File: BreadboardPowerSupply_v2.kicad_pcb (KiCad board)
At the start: 2 copper layers, 30.1 x 52.2 mm, 15 parts, among them J1 Barrel_Jack_Switch, J2 Conn_02x02_Odd_Even, J3 Conn_02x02_Odd_Even, SW1 SW_DPDT_x2, U1 LM7805_TO220

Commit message: Placement completed.
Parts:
- C1: footprint Capacitor_THT:CP_Radial_D10.0mm_P5.00mm_P7.50mm -> Capacitor_THT:CP_Radial_D10.0mm_P5.00mm
- moved C1 48.8 mm to (43.3, 110.6), turned to 270 degrees
- moved D1 10.9 mm to (39.1, 144.7)
- moved D4 10.5 mm to (39.1, 130.4)
- moved R2 7.62 mm to (50.8, 119.6), turned to 270 degrees
- moved D2 4.62 mm to (39.1, 139.9)
- moved U1 4.57 mm to (40.6, 123.7)
- moved C2 2.22 mm to (54.2, 112.0), turned to 270 degrees
- moved D3 2.16 mm to (39.1, 135.2)
- moved D6 0.13 mm to (55.0, 121.8)

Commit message: Added additional net names for power.
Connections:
- net /Vout renamed /Vout1
- net Net-(D1-Pad2) renamed /V1
- net Net-(D3-Pad2) renamed /V2
- net Net-(J2-Pad1) renamed /Vout2
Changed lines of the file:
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@@
   (net 1 /Vin)
   (net 2 /V-)
-  (net 3 /Vout)
-  (net 4 "Net-(D1-Pad2)")
-  (net 5 "Net-(D3-Pad2)")
-  (net 6 "Net-(D5-Pad2)")
-  (net 7 "Net-(D6-Pad2)")
-  (net 8 "Net-(J1-Pad3)")
-  (net 9 "Net-(J2-Pad1)")
-  (net 10 "Net-(SW1-Pad3)")
+  (net 3 "Net-(D5-Pad2)")
+  (net 4 "Net-(D6-Pad2)")
+  (net 5 "Net-(J1-Pad3)")
+  (net 6 "Net-(SW1-Pad3)")
+  (net 7 /V1)
+  (net 8 /V2)
+  (net 9 /Vout2)
+  (net 10 /Vout1)
   (net_class Default "This is the default net class."
     (clearance 0.2)
@@
     (uvia_drill 0.1)
     (add_net /V-)
+    (add_net /V1)
+    (add_net /V2)
     (add_net /Vin)
-    (add_net /Vout)
-    (add_net "Net-(D1-Pad2)")
-    (add_net "Net-(D3-Pad2)")
+    (add_net /Vout1)
+    (add_net /Vout2)
     (add_net "Net-(D5-Pad2)")
     (add_net "Net-(D6-Pad2)")
     (add_net "Net-(J1-Pad3)")
-    (add_net "Net-(J2-Pad1)")
     (add_net "Net-(SW1-Pad3)")
   )
@@
     )
     (pad 1 thru_hole rect (at 0 0 270) (size 1.6 1.6) (drill 0.8) (layers *.Cu *.Mask)
-      (net 3 /Vout))
+      (net 10 /Vout1))
     (pad 2 thru_hole circle (at 2.5 0 270) (size 1.6 1.6) (drill 0.8) (layers *.Cu *.Mask)
       (net 2 /V-))
@@
       (net 1 /Vin))
     (pad 2 thru_hole oval (at 10.16 0) (size 2.2 2.2) (drill 1.1) (layers *.Cu *.Mask)
-      (net 4 "Net-(D1-Pad2)"))
+      (net 7 /V1))
     (model ${KISYS3DMOD}/Diode_THT.3dshapes/D_DO-41_SOD81_P10.16mm_Horizontal.wrl
       (at (xyz 0 0 0))
@@
       (net 2 /V-))
     (pad 1 thru_hole rect (at 0 0) (size 2.2 2.2) (drill 1.1) (layers *.Cu *.Mask)
-      (net 4 "Net-(D1-Pad2)"))
+      (net 7 /V1))
     (model ${KISYS3DMOD}/Diode_THT.3dshapes/D_DO-41_SOD81_P10.16mm_Horizontal.wrl
       (at (xyz 0 0 0))
@@
       (net 1 /Vin))
     (pad 2 thru_hole oval (at 10.16 0) (size 2.2 2.2) (drill 1.1) (layers *.Cu *.Mask)
-      (net 5 "Net-(D3-Pad2)"))
+      (net 8 /V2))
     (model ${KISYS3DMOD}/Diode_THT.3dshapes/D_DO-41_SOD81_P10.16mm_Horizontal.wrl
       (at (xyz 0 0 0))
@@
       (net 2 /V-))
     (pad 1 thru_hole rect (at 0 0) (size 2.2 2.2) (drill 1.1) (layers *.Cu *.Mask)
-      (net 5 "Net-(D3-Pad2)"))
+      (net 8 /V2))
     (model ${KISYS3DMOD}/Diode_THT.3dshapes/D_DO-41_SOD81_P10.16mm_Horizontal.wrl
       (at (xyz 0 0 0))
@@
     (fp_arc (start 1.27 0) (end -1.23 -1.469694) (angle 299.1) (layer F.Fab) (width 0.1))
     (pad 2 thru_hole circle (at 2.54 0) (size 1.8 1.8) (drill 0.9) (layers *.Cu *.Mask)
-      (net 6 "Net-(D5-Pad2)"))
+      (net 3 "Net-(D5-Pad2)"))
     (pad 1 thru_hole rect (at 0 0) (size 1.8 1.8) (drill 0.9) (layers *.Cu *.Mask)
       (net 2 /V-))
@@
       (net 2 /V-))
     (pad 2 thru_hole circle (at 2.54 0) (size 1.8 1.8) (drill 0.9) (layers *.Cu *.Mask)
-      (net 7 "Net-(D6-Pad2)"))
+      (net 4 "Net-(D6-Pad2)"))
     (model ${KISYS3DMOD}/LED_THT.3dshapes/LED_D5.0mm.wrl
       (at (xyz 0 0 0))
@@
     (fp_line (start -4.5 10.2) (end 4.5 10.2) (layer F.Fab) (width 0.1))
     (pad 1 thru_hole rect (at 0 0 270) (size 2.6 2.6) (drill 1.6) (layers *.Cu *.Mask)
-      (net 4 "Net-(D1-Pad2)"))
+      (net 7 /V1))
     (pad 2 thru_hole circle (at 0 6 270) (size 2.6 2.6) (drill 1.6) (layers *.Cu *.Mask)
-      (net 5 "Net-(D3-Pad2)"))
+      (net 8 /V2))
     (pad 3 thru_hole circle (at 4.7 3 270) (size 2.6 2.6) (drill 1.6) (layers *.Cu *.Mask)
-      (net 8 "Net-(J1-Pad3)"))
+      (net 5 "Net-(J1-Pad3)"))
     (model ${KISYS3DMOD}/Connector_BarrelJack.3dshapes/BarrelJack_CUI_PJ-102AH_Horizontal.wrl
       (at (xyz 0 0 0))
@@
       (net 2 /V-))
     (pad 2 thru_hole oval (at 2.54 0 180) (size 1.7 1.7) (drill 1) (layers *.Cu *.Mask)
-      (net 9 "Net-(J2-Pad1)"))
+      (net 9 /Vout2))
     (pad 1 thru_hole rect (at 0 0 180) (size 1.7 1.7) (drill 1) (layers *.Cu *.Mask)
-      (net 9 "Net-(J2-Pad1)"))
+      (net 9 /Vout2))
     (model ${KISYS3DMOD}/Connector_PinHeader_2.54mm.3dshapes/PinHeader_2x02_P2.54mm_Vertical.wrl
       (at (xyz 0 0 0))
@@
     )
     (pad 1 thru_hole rect (at 0 0 180) (size 1.7 1.7) (drill 1) (layers *.Cu *.Mask)
-      (net 9 "Net-(J2-Pad1)"))
+      (net 9 /Vout2))
     (pad 2 thru_hole oval (at 2.54 0 180) (size 1.7 1.7) (drill 1) (layers *.Cu *.Mask)
-      (net 9 "Net-(J2-Pad1)"))
+      (net 9 /Vout2))
     (pad 3 thru_hole oval (at 0 2.54 180) (size 1.7 1.7) (drill 1) (layers *.Cu *.Mask)
       (net 2 /V-))
@@
     )
     (pad 1 thru_hole circle (at 0 0 90) (size 1.6 1.6) (drill 0.8) (layers *.Cu *.Mask)
-      (net 3 /Vout))
+      (net 10 /Vout1))
     (pad 2 thru_hole oval (at 7.62 0 90) (size 1.6 1.6) (drill 0.8) (layers *.Cu *.Mask)
-      (net 6 "Net-(D5-Pad2)"))
+      (net 3 "Net-(D5-Pad2)"))
     (model ${KISYS3DMOD}/Resistor_THT.3dshapes/R_Axial_DIN0207_L6.3mm_D2.5mm_P7.62mm_Horizontal.wrl
       (at (xyz 0 0 0))
@@
     (fp_line (start 0.66 -1.25) (end 0.66 1.25) (layer F.Fab) (width 0.1))
     (pad 2 thru_hole oval (at 7.62 0 270) (size 1.6 1.6) (drill 0.8) (layers *.Cu *.Mask)
-      (net 7 "Net-(D6-Pad2)"))
+      (net 4 "Net-(D6-Pad2)"))
     (pad 1 thru_hole circle (at 0 0 270) (size 1.6 1.6) (drill 0.8) (layers *.Cu *.Mask)
-      (net 9 "Net-(J2-Pad1)"))
+      (net 9 /Vout2))
     (model ${KISYS3DMOD}/Resistor_THT.3dshapes/R_Axial_DIN0207_L6.3mm_D2.5mm_P7.62mm_Horizontal.wrl
       (at (xyz 0 0 0))
@@
     (fp_line (start -3.42 -2) (end 8.18 -2) (layer F.Fab) (width 0.1))
     (pad 1 thru_hole rect (at 0 0 90) (size 1.9 1.9) (drill 0.9) (layers *.Cu *.Mask)
-      (net 9 "Net-(J2-Pad1)"))
+      (net 9 /Vout2))
     (pad 2 thru_hole circle (at 2.5 0 90) (size 1.9 1.9) (drill 0.9) (layers *.Cu *.Mask)
-      (net 3 /Vout))
+      (net 10 /Vout1))
     (pad 3 thru_hole circle (at 5 0 90) (size 1.9 1.9) (drill 0.9) (layers *.Cu *.Mask)
-      (net 10 "Net-(SW1-Pad3)"))
+      (net 6 "Net-(SW1-Pad3)"))
   )
   (module Package_TO_SOT_THT:TO-220-3_Vertical (layer F.Cu)
@@
       (net 2 /V-))
     (pad 3 thru_hole oval (at 5.08 0) (size 1.905 2) (drill 1.1) (layers *.Cu *.Mask)
-      (net 3 /Vout))
+      (net 10 /Vout1))
     (model ${KISYS3DMOD}/Package_TO_SOT_THT.3dshapes/TO-220-3_Vertical.wrl
       (at (xyz 0 0 0))

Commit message: Tracing is complete.
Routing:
- net /V-: track 0.00 -> 89.2 mm
- net /Vout2: track 0.00 -> 69.1 mm
- net /Vout1: track 0.00 -> 59.3 mm
- net /Vin: track 0.00 -> 39.6 mm
- net /V2: track 0.00 -> 30.3 mm
- net /V1: track 0.00 -> 21.0 mm
- net Net-(D6-Pad2): track 0.00 -> 9.74 mm
- net Net-(D5-Pad2): track 0.00 -> 7.17 mm
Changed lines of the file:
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@@
     (thickness 1.6)
     (drawings 13)
-    (tracks 0)
+    (tracks 93)
     (zones 0)
     (modules 15)
@@
     (uvia_dia 0.3)
     (uvia_drill 0.1)
-    (add_net /V-)
-    (add_net /V1)
-    (add_net /V2)
-    (add_net /Vin)
-    (add_net /Vout1)
-    (add_net /Vout2)
     (add_net "Net-(D5-Pad2)")
     (add_net "Net-(D6-Pad2)")
@@
     (uvia_dia 0.3)
     (uvia_drill 0.1)
+    (add_net /V-)
+    (add_net /V1)
+    (add_net /V2)
+    (add_net /Vin)
+    (add_net /Vout1)
+    (add_net /Vout2)
   )
   (module Capacitor_THT:CP_Radial_D6.3mm_P2.50mm (layer F.Cu)
@@
   (gr_line (start 36.957 159.385) (end 67.056 159.385) (layer Edge.Cuts) (width 0.15))
   (gr_line (start 36.957 107.188) (end 36.957 159.385) (layer Edge.Cuts) (width 0.15))
+  (segment (start 37.48201 141.61901) (end 39.116 143.253) (width 0.3) (layer F.Cu) (net 1))
+  (segment (start 37.48201 138.204323) (end 37.48201 141.61901) (width 0.3) (layer F.Cu) (net 1))
+  (segment (start 39.116 136.570333) (end 37.48201 138.204323) (width 0.3) (layer F.Cu) (net 1))
+  (segment (start 39.116 143.253) (end 39.116 144.653) (width 0.3) (layer F.Cu) (net 1))
+  (segment (start 39.116 135.170333) (end 39.116 136.570333) (width 0.3) (layer F.Cu) (net 1))
+  (segment (start 39.116 133.770333) (end 42.164 130.722333) (width 0.3) (layer F.Cu) (net 1))
+  (segment (start 39.116 135.170333) (end 39.116 133.770333) (width 0.3) (layer F.Cu) (net 1))
+  (segment (start 42.164 130.722333) (end 42.164 127.889) (width 0.3) (layer F.Cu) (net 1))
+  (segment (start 40.64 126.365) (end 40.64 123.698) (width 0.3) (layer F.Cu) (net 1))
+  (segment (start 42.164 127.889) (end 40.64 126.365) (width 0.3) (layer F.Cu) (net 1))
+  (segment (start 42.007 110.617) (end 43.307 110.617) (width 0.3) (layer F.Cu) (net 1))
+  (segment (start 40.132 112.649) (end 41.783 110.998) (width 0.3) (layer F.Cu) (net 1))
+  (segment (start 40.64 122.398) (end 40.132 121.89) (width 0.3) (layer F.Cu) (net 1))
+  (segment (start 40.64 123.698) (end 40.64 122.398) (width 0.3) (layer F.Cu) (net 1))
+  (segment (start 40.132 121.89) (end 40.132 112.649) (width 0.3) (layer F.Cu) (net 1))
+  (segment (start 41.783 110.841) (end 42.007 110.617) (width 0.3) (layer F.Cu) (net 1))
+  (segment (start 41.783 110.998) (end 41.783 110.841) (width 0.3) (layer F.Cu) (net 1))
+  (segment (start 43.18 124.333) (end 43.18 123.698) (width 0.3) (layer B.Cu) (net 2))
+  (segment (start 49.276 130.429) (end 43.18 124.333) (width 0.3) (layer B.Cu) (net 2))
+  (segment (start 54.991 140.786) (end 54.991 141.986) (width 0.3) (layer B.Cu) (net 2))
+  (segment (start 54.116666 139.911666) (end 54.991 140.786) (width 0.3) (layer B.Cu) (net 2))
+  (segment (start 49.276 139.911666) (end 54.116666 139.911666) (width 0.3) (layer B.Cu) (net 2))
+  (segment (start 54.991 143.186) (end 59.055 147.25) (width 0.3) (layer B.Cu) (net 2))
+  (segment (start 54.991 141.986) (end 54.991 143.186) (width 0.3) (layer B.Cu) (net 2))
+  (segment (start 59.055 152.126476) (end 59.69 152.761476) (width 0.3) (layer B.Cu) (net 2))
+  (segment (start 59.055 147.25) (end 59.055 152.126476) (width 0.3) (layer B.Cu) (net 2))
+  (segment (start 59.69 152.761476) (end 59.69 153.797) (width 0.3) (layer B.Cu) (net 2))
+  (segment (start 60.579 154.686) (end 62.484 154.686) (width 0.3) (layer B.Cu) (net 2))
+  (segment (start 59.69 153.797) (end 60.579 154.686) (width 0.3) (layer B.Cu) (net 2))
+  (segment (start 62.484 154.686) (end 65.024 154.686) (width 0.3) (layer B.Cu) (net 2))
+  (segment (start 50.826001 138.361665) (end 50.826001 137.260999) (width 0.3) (layer B.Cu) (net 2))
+  (segment (start 49.276 139.911666) (end 50.826001 138.361665) (width 0.3) (layer B.Cu) (net 2))
+  (segment (start 50.826001 137.260999) (end 52.451 135.636) (width 0.3) (layer B.Cu) (net 2))
+  (segment (start 52.451 133.604) (end 49.276 130.429) (width 0.3) (layer B.Cu) (net 2))
+  (segment (start 52.451 135.636) (end 52.451 133.604) (width 0.3) (layer B.Cu) (net 2))
+  (segment (start 49.276 128.873366) (end 49.022 128.619366) (width 0.3) (layer B.Cu) (net 2))
+  (segment (start 49.276 130.429) (end 49.276 128.873366) (width 0.3) (layer B.Cu) (net 2))
+  (segment (start 49.022 128.619366) (end 49.022 125.349) (width 0.3) (layer B.Cu) (net 2))
+  (segment (start 52.578 121.793) (end 54.991 121.793) (width 0.3) (layer B.Cu) (net 2))
+  (segment (start 49.022 125.349) (end 52.578 121.793) (width 0.3) (layer B.Cu) (net 2))
+  (segment (start 54.991 115.276) (end 54.229 114.514) (width 0.3) (layer B.Cu) (net 2))
+  (segment (start 54.991 121.793) (end 54.991 115.276) (width 0.3) (layer B.Cu) (net 2))
+  (segment (start 43.18 115.744) (end 43.307 115.617) (width 0.3) (layer B.Cu) (net 2))
+  (segment (start 43.18 123.698) (end 43.18 115.744) (width 0.3) (layer B.Cu) (net 2))
+  (segment (start 54.229 114.514) (end 55.92 114.514) (width 0.3) (layer B.Cu) (net 2))
+  (segment (start 55.92 114.514) (end 60.706 109.728) (width 0.3) (layer B.Cu) (net 2))
+  (segment (start 60.706 109.728) (end 62.484 109.728) (width 0.3) (layer B.Cu) (net 2))
+  (segment (start 62.484 109.728) (end 65.024 109.728) (width 0.3) (layer B.Cu) (net 2))
+  (segment (start 56.769 148.844) (end 56.769 145.542) (width 0.25) (layer F.Cu) (net 3))
+  (segment (start 57.531 144.78) (end 57.531 141.986) (width 0.25) (layer F.Cu) (net 3))
+  (segment (start 56.769 145.542) (end 57.531 144.78) (width 0.25) (layer F.Cu) (net 3))
+  (segment (start 57.531 123.065792) (end 56.769 123.827792) (width 0.25) (layer F.Cu) (net 4))
+  (segment (start 57.531 121.793) (end 57.531 123.065792) (width 0.25) (layer F.Cu) (net 4))
+  (segment (start 54.226208 123.827792) (end 50.8 127.254) (width 0.25) (layer F.Cu) (net 4))
+  (segment (start 56.769 123.827792) (end 54.226208 123.827792) (width 0.25) (layer F.Cu) (net 4))
+  (segment (start 51.435 146.812) (end 49.276 144.653) (width 0.3) (layer F.Cu) (net 7))
+  (segment (start 51.435 152.654) (end 51.435 146.812) (width 0.3) (layer F.Cu) (net 7))
+  (segment (start 44.534666 139.911666) (end 39.116 139.911666) (width 0.3) (layer F.Cu) (net 7))
+  (segment (start 49.276 144.653) (end 44.534666 139.911666) (width 0.3) (layer F.Cu) (net 7))
+  (segment (start 45.435 139.011333) (end 49.276 135.170333) (width 0.3) (layer B.Cu) (net 8))
+  (segment (start 45.435 152.654) (end 45.435 139.011333) (width 0.3) (layer B.Cu) (net 8))
+  (segment (start 45.435 138.148) (end 45.435 139.011333) (width 0.3) (layer B.Cu) (net 8))
+  (segment (start 39.116 131.829) (end 45.435 138.148) (width 0.3) (layer B.Cu) (net 8))
+  (segment (start 39.116 130.429) (end 39.116 131.829) (width 0.3) (layer B.Cu) (net 8))
+  (segment (start 51.599999 118.834001) (end 54.774999 118.834001) (width 0.3) (layer F.Cu) (net 9))
+  (segment (start 50.8 119.634) (end 51.599999 118.834001) (width 0.3) (layer F.Cu) (net 9))
+  (segment (start 54.774999 118.834001) (end 59.309 114.3) (width 0.3) (layer F.Cu) (net 9))
+  (segment (start 59.309 114.3) (end 59.309 113.284) (width 0.3) (layer F.Cu) (net 9))
+  (segment (start 60.325 112.268) (end 62.484 112.268) (width 0.3) (layer F.Cu) (net 9))
+  (segment (start 59.309 113.284) (end 60.325 112.268) (width 0.3) (layer F.Cu) (net 9))
+  (segment (start 62.484 112.268) (end 65.024 112.268) (width 0.3) (layer F.Cu) (net 9))
+  (segment (start 59.309 132.441) (end 59.309 114.3) (width 0.3) (layer F.Cu) (net 9))
+  (segment (start 57.511 134.239) (end 59.309 132.441) (width 0.3) (layer F.Cu) (net 9))
+  (segment (start 56.261 134.239) (end 57.511 134.239) (width 0.3) (layer F.Cu) (net 9))
+  (segment (start 59.309 155.253081) (end 59.309 132.441) (width 0.3) (layer F.Cu) (net 9))
+  (segment (start 61.281919 157.226) (end 59.309 155.253081) (width 0.3) (layer F.Cu) (net 9))
+  (segment (start 62.484 157.226) (end 61.281919 157.226) (width 0.3) (layer F.Cu) (net 9))
+  (segment (start 65.024 157.226) (end 62.484 157.226) (width 0.3) (layer F.Cu) (net 9))
+  (segment (start 45.72 122.398) (end 45.72 123.698) (width 0.3) (layer F.Cu) (net 10))
+  (segment (start 45.72 119.423) (end 45.72 122.398) (width 0.3) (layer F.Cu) (net 10))
+  (segment (start 53.129 112.014) (end 45.72 119.423) (width 0.3) (layer F.Cu) (net 10))
+  (segment (start 54.229 112.014) (end 53.129 112.014) (width 0.3) (layer F.Cu) (net 10))
+  (segment (start 45.72 124.998) (end 45.72 123.698) (width 0.3) (layer F.Cu) (net 10))
+  (segment (start 49.600999 128.878999) (end 45.72 124.998) (width 0.3) (layer F.Cu) (net 10))
+  (segment (start 53.400999 128.878999) (end 49.600999 128.878999) (width 0.3) (layer F.Cu) (net 10))
+  (segment (start 56.261 131.739) (end 53.400999 128.878999) (width 0.3) (layer F.Cu) (net 10))
+  (segment (start 56.769 155.33263) (end 53.975 152.53863) (width 0.3) (layer F.Cu) (net 10))
+  (segment (start 56.769 156.464) (end 56.769 155.33263) (width 0.3) (layer F.Cu) (net 10))
+  (segment (start 53.975 152.53863) (end 53.975 146.177) (width 0.3) (layer F.Cu) (net 10))
+  (segment (start 53.975 146.177) (end 52.832 145.034) (width 0.3) (layer F.Cu) (net 10))
+  (segment (start 52.832 145.034) (end 52.832 133.35) (width 0.3) (layer F.Cu) (net 10))
+  (segment (start 54.443 131.739) (end 56.261 131.739) (width 0.3) (layer F.Cu) (net 10))
+  (segment (start 52.832 133.35) (end 54.443 131.739) (width 0.3) (layer F.Cu) (net 10))
 )

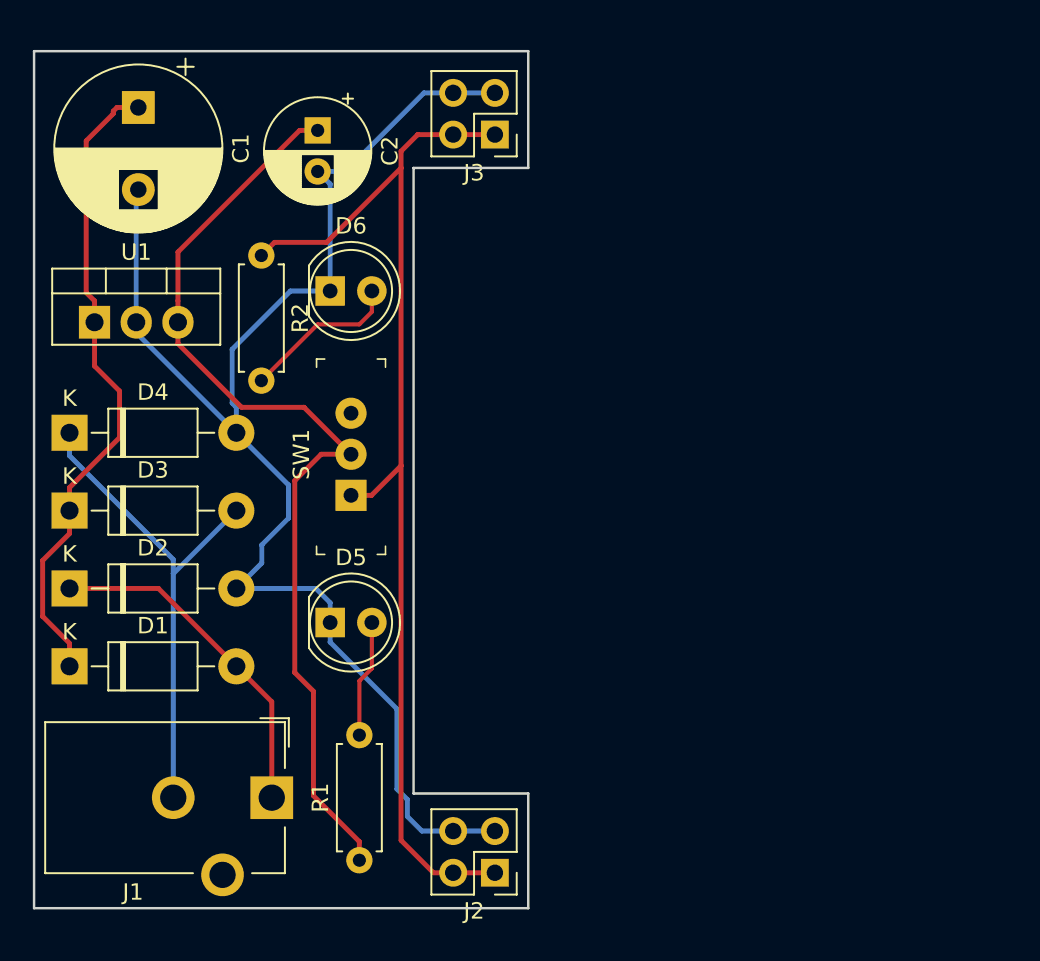
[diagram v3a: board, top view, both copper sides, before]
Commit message: Added silkscreen logos.
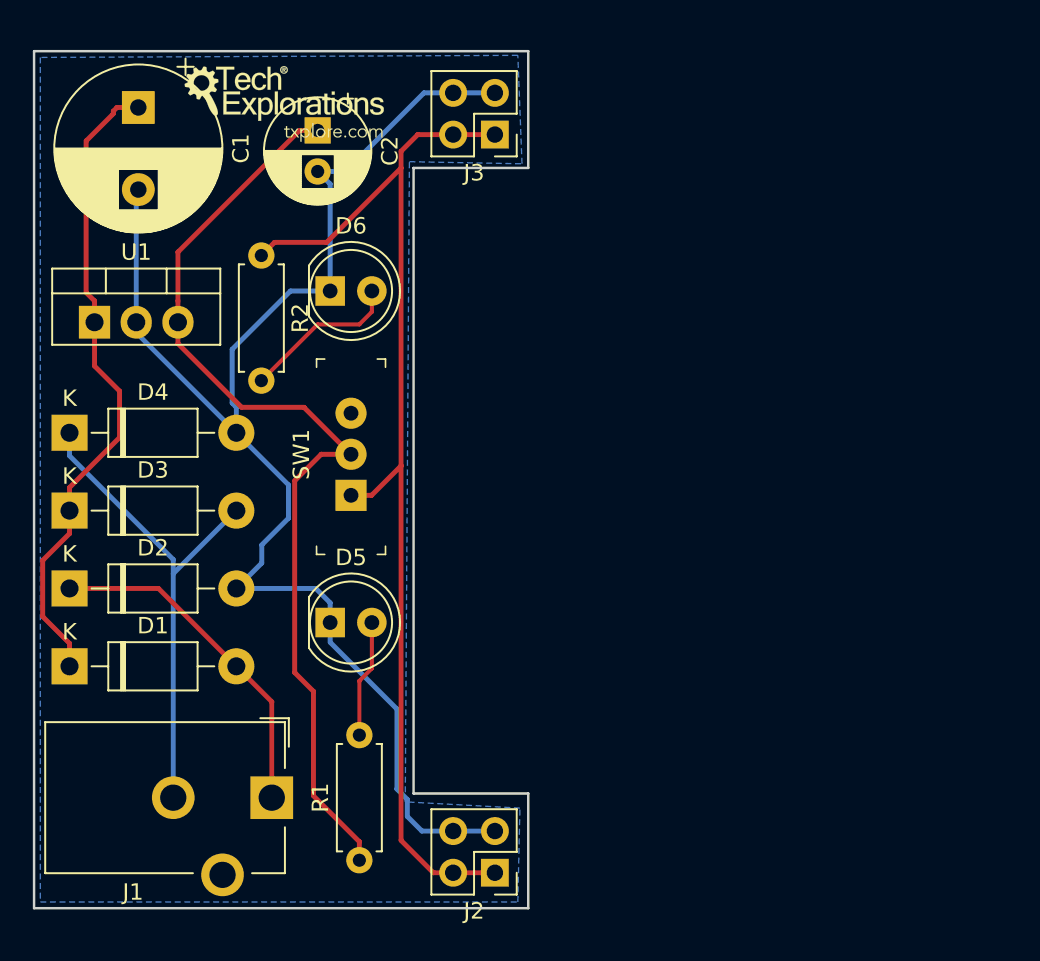
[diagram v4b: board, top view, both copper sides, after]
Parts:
- added G***: LOGO, Custom libraries:TE_Logo_12mm, F.Cu at (52.2, 110.4)
- added G***: LOGO, Custom libraries:TE_LOGO_URL_v2, B.Cu at (44.6, 135.5)
- added REF**: KiCad-Logo2_8mm_SilkScreen, Symbol:KiCad-Logo2_8mm_SilkScreen, B.Cu at (46.4, 111.9)
- added REF**: OSHW-Logo2_7.3x6mm_SilkScreen, Symbol:OSHW-Logo2_7.3x6mm_SilkScreen, B.Cu at (41.0, 119.0)
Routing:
- added copper zone on B.Cu, net /V-
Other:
- board text added: "Breadboard Power Supply v2"
- board text added: "peter@txplore.com"
